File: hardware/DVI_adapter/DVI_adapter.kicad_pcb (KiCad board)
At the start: 2 copper layers, 34.6 x 28.4 mm, 51 parts, among them J1 DF12NB(3.0)-30DS-0.5V(51), J2 DF12NB(3.0)-30DS-0.5V(51), J3 FPC Cable connector 1x20, U2 TXS0102DQMR, U3 TFP410

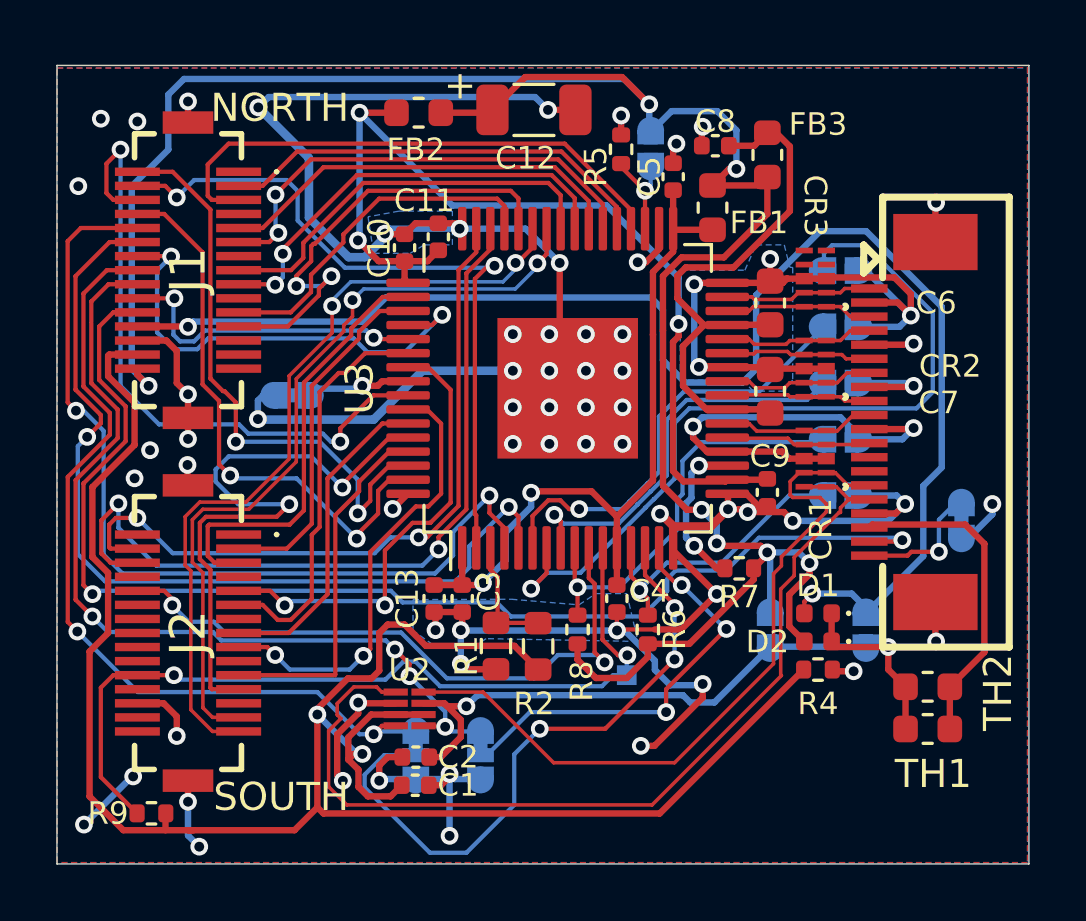
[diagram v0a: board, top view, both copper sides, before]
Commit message: Change to 4 layers for better signal integrity. Reorganize differential pins in SSG format to minimize crosstalk at output connector (pinout compatible with common extension cables). Fix level translator footpriont. Add power plane, test points, 5V charge pump, auto reset
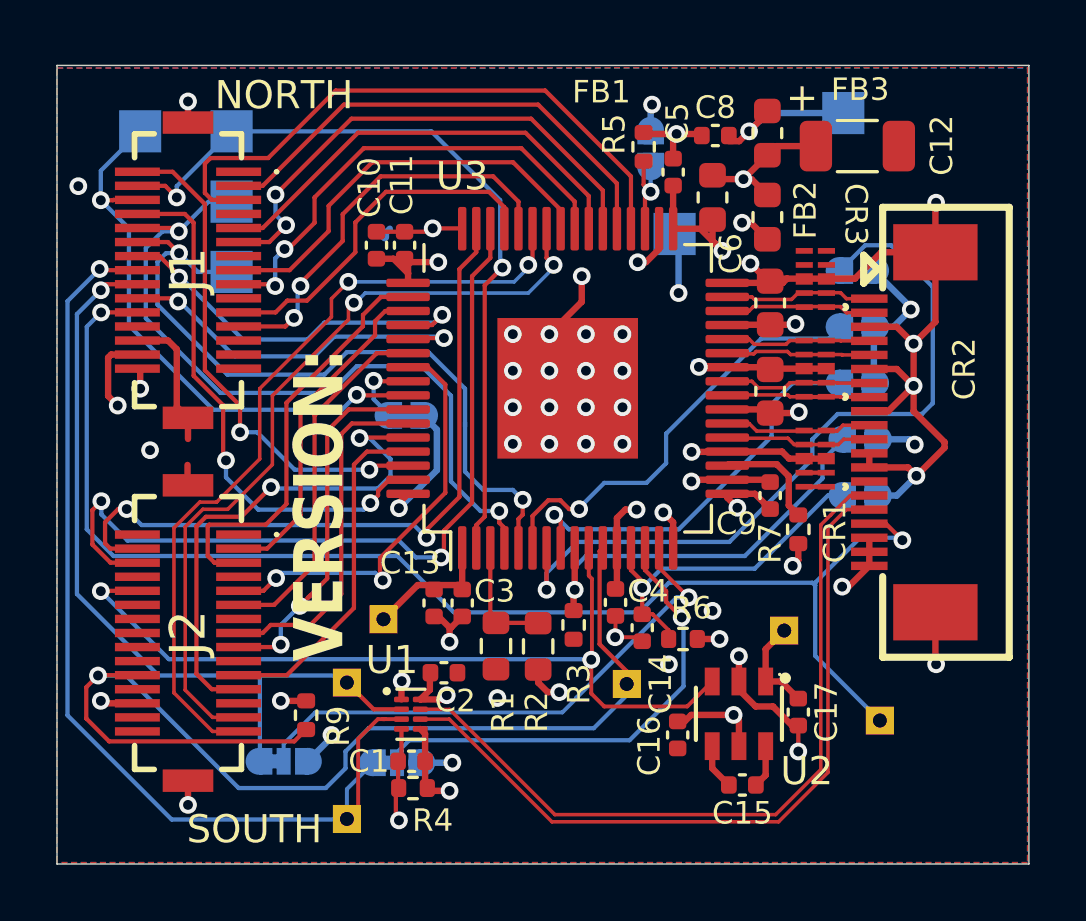
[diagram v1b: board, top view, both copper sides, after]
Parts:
- removed D1, D2: NSR05F40NXT5G, Diode_SMD:D_0402_1005Metric
- removed JP10, JP11: JMP_ISEL, Library:SolderJumper-2_Open_RoundedPad_2.254x0.95mm
- removed JP12: JMP_CKn, Library:SolderJumper-2_Closed_RoundedPad_2.254x0.95mm
- removed R8: 10K, Resistor_SMD:R_0402_1005Metric
- removed TH1, TH2: PRG18BB330MB1RB, Fuse:Fuse_0603_1608Metric
- added C14: 0.1uF, Library:C_0402_1005Metric, F.Cu at (124.5, 132.9)
- added C15: 2.2uF, Library:C_0402_1005Metric, F.Cu at (128.1, 138.5)
- added C16: 2.2uF, Library:C_0402_1005Metric, F.Cu at (125.8, 136.7)
- added C17: 2.2uF, Library:C_0402_1005Metric, F.Cu at (130.1, 135.9)
- added R3: 10K, Resistor_SMD:R_0402_1005Metric, F.Cu at (122.1, 132.8)
- added TP10: TP_SDA, TestPoint:TestPoint_THTPad_1.0x1.0mm_Drill0.5mm, B.Cu at (114.0, 139.7)
- added TP11: TP_SCK, TestPoint:TestPoint_THTPad_1.0x1.0mm_Drill0.5mm, B.Cu at (114.0, 134.8)
- added TP12: TP_HPD, TestPoint:TestPoint_THTPad_1.0x1.0mm_Drill0.5mm, B.Cu at (133.0, 136.2)
- added TP2: TP_DE, TestPoint:TestPoint_Pad_1.5x1.5mm, B.Cu at (110.0, 115.2)
- added TP3: TP_HS, TestPoint:TestPoint_Pad_1.5x1.5mm, B.Cu at (110.0, 117.8)
- added TP4: TP_VS, TestPoint:TestPoint_Pad_1.5x1.5mm, B.Cu at (110.0, 120.2)
- added TP5: TP_PCLK, TestPoint:TestPoint_Pad_1.5x1.5mm, B.Cu at (106.7, 115.2)
- added TP6: TP_PVDD, TestPoint:TestPoint_Pad_1.5x1.5mm, B.Cu at (125.7, 118.9)
- added TP7: TP_DVDD, TestPoint:TestPoint_THTPad_1.0x1.0mm_Drill0.5mm, B.Cu at (115.3, 132.6)
- added TP8: TP_TVDD, TestPoint:TestPoint_Pad_1.5x1.5mm, B.Cu at (131.7, 114.6)
- added TP9: TP_VDVI, TestPoint:TestPoint_THTPad_1.0x1.0mm_Drill0.5mm, B.Cu at (129.6, 133.0)
- added U1: TXS0102DQE, Package_SON:X2SON-8_1.4x1mm_P0.35mm, F.Cu at (116.3, 136.0)
- U2: value TXS0102DQMR -> HE9009M6R; footprint Library:DQM8 -> easyeda2kicad:SOT-23-6_L2.9-W1.7-P0.95-LS2.8-BL
- moved R4 15.0 mm to (116.4, 138.6), turned to 180 degrees
- moved G*** 13.2 mm to (107.0, 128.2), turned to 90 degrees
- moved FB2 12.9 mm to (129.0, 118.3), turned to -90 degrees
- moved U2 11.7 mm to (128.0, 136.0), turned to 180 degrees
- moved C12 11.6 mm to (132.2, 115.8)
- moved JP8 7.00 mm to (111.8, 137.7), turned to 0 degrees
- moved R9 6.51 mm to (112.6, 136.0), turned to -90 degrees
- moved JP9 4.12 mm to (116.2, 125.3), turned to 180 degrees
- moved C2 3.16 mm to (117.5, 134.5), turned to 0 degrees
- moved G*** 2.80 mm to (136.2, 117.0), turned to 90 degrees
- moved R7 2.52 mm to (130.1, 129.4), turned to -90 degrees
- moved R6 1.29 mm to (126.0, 133.3), turned to 0 degrees
- moved C11 1.24 mm to (116.1, 119.3)
- moved C10 1.00 mm to (115.1, 119.3)
- moved C1 0.86 mm to (116.3, 137.7), turned to 180 degrees
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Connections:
- CR1 pad 1: SDA_SHIFTED -> Net-(CR1-Pad1)
- CR1 pad 10: SDA_SHIFTED -> Net-(CR1-Pad1)
- CR1 pad 2: SCK_SHIFTED -> Net-(CR1-Pad2)
- CR1 pad 9: SCK_SHIFTED -> Net-(CR1-Pad2)
- J3 pad 11: GND -> /TXC-
- J3 pad 12: /TXC- -> GND
- J3 pad 13: unconnected-(J3-Pad13) -> GND
- J3 pad 17: GND -> HPD
- J3 pad 18: V_DVI_OUT -> V_DVI
- J3 pad 19: HPD -> V_DVI
- J3 pad 2: GND -> /TX2-
- J3 pad 20: Net-(JP12-B) -> V_DVI
- J3 pad 3: /TX2- -> GND
- J3 pad 5: GND -> /TX1-
- J3 pad 6: /TX1- -> GND
- J3 pad 8: GND -> /TX0-
- J3 pad 9: /TX0- -> GND
- JP1 pad 1: GND -> +3V3
- JP2 pad 1: GND -> +3V3
- JP3 pad 1: GND -> +3V3
- JP6 pad 1: GND -> +3V3
- U2 pad 1: SDA_SHIFTED -> V_DVI
- U2 pad 3: VCC3V3 -> PSEL
- U2 pad 4: SDA -> Net-(U2-CN)
- U2 pad 5: SCK -> +3V3
- U2 pad 6: VCC3V3 -> Net-(U2-CP)
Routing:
- net GND: track 166.2 -> 83.5 mm, vias 70 -> 46
- net VCCIN: track 51.4 -> 0.00 mm, vias 2 -> 0
- net VCC3V3: track 71.0 -> 39.8 mm, vias 2 -> 5
- net V_DVI_OUT: track 11.5 -> 0.00 mm
- net DVDD: track 26.7 -> 36.4 mm
- net HPD2: track 29.8 -> 39.3 mm, vias 2 -> 1
- net SDA_SHIFTED: track 34.7 -> 27.2 mm
- net PSEL: track 22.8 -> 30.0 mm
- net SDA: track 29.9 -> 36.5 mm, vias 2 -> 1
- net Net-(JP7-C): track 22.8 -> 17.0 mm, vias 3 -> 1
- net LCD_VSYNC: track 32.2 -> 26.4 mm
- net LCD_HSYNC: track 32.2 -> 27.1 mm
- net Net-(JP8-C): track 15.1 -> 19.8 mm, vias 3 -> 1
- net Net-(JP12-B): track 4.70 -> 0.00 mm, vias 1 -> 0
- net HPD: track 44.1 -> 48.0 mm
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- added copper zone on In2.Cu, net +3V3
- added copper zone on In2.Cu, net DVDD
- added copper zone on In1.Cu, net GND
- added copper zone on In2.Cu, net PVDD
- added copper zone on In2.Cu, net TVDD
- added copper zone on In2.Cu, net VCC3V3
- added copper zone on In2.Cu, net V_DVI
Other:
- copper layers 2 -> 4
- board text added: "DVI Adapter V0.1"
- board text added: "VERSION:"
- board text removed: "DVI Adapter V0.09"

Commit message: improve power plane in DVI adapter
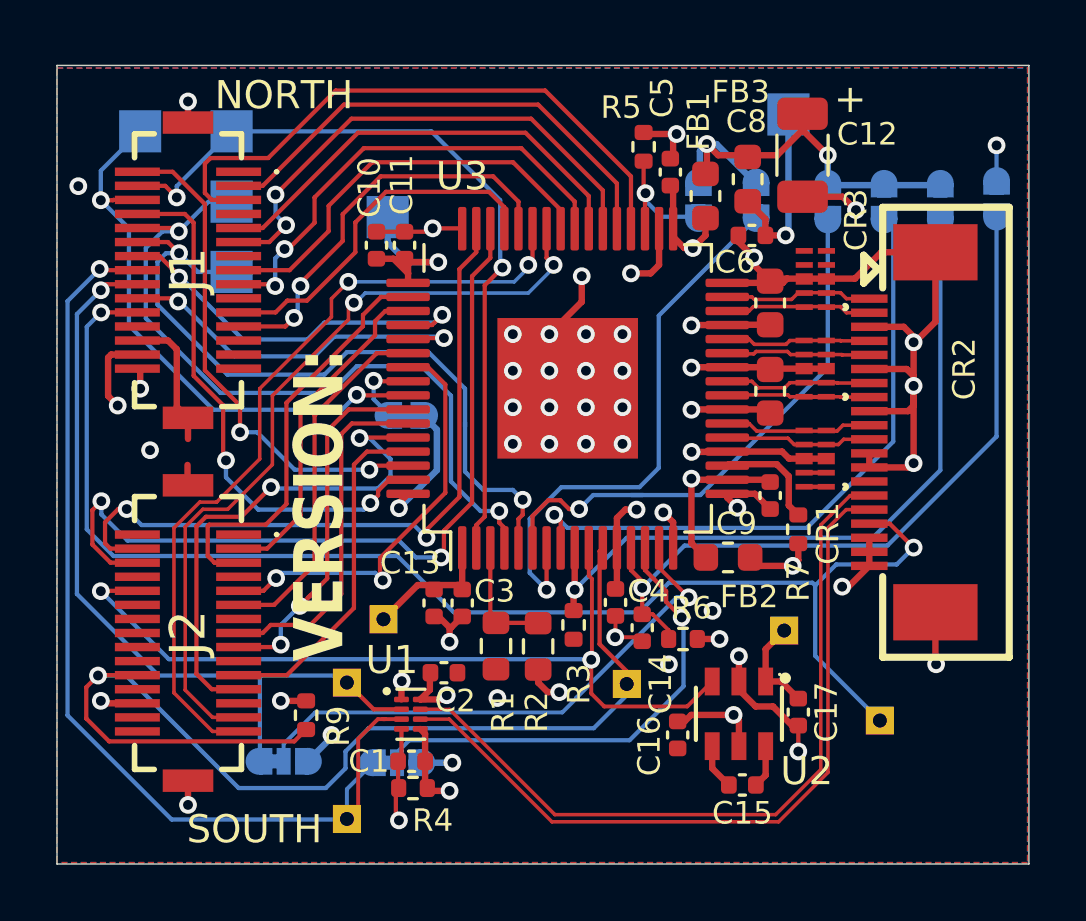
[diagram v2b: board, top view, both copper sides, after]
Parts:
- moved FB2 12.2 mm to (127.6, 130.4), turned to 180 degrees
- moved JP5 11.6 mm to (137.2, 117.7), turned to -90 degrees
- moved TP6 10.2 mm to (115.5, 118.3)
- moved JP6 8.92 mm to (135.2, 117.8), turned to -90 degrees
- moved JP3 6.52 mm to (133.2, 117.8), turned to -90 degrees
- moved JP1 4.57 mm to (131.2, 117.8), turned to -90 degrees
- moved JP2 4.38 mm to (128.6, 117.7), turned to -90 degrees
- moved C8 3.78 mm to (128.4, 119.0)
- moved G*** 2.78 mm to (134.8, 114.6), turned to 180 degrees
- moved JP4 2.50 mm to (126.5, 117.7)
- moved C12 1.98 mm to (130.2, 116.1), turned to -90 degrees
- moved TP8 1.95 mm to (129.8, 114.7)
- moved FB3 1.78 mm to (128.3, 117.0), turned to -90 degrees
- moved FB1 0.25 mm to (126.8, 117.5)
- moved C5 0.10 mm to (125.5, 116.7)
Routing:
- net +3V3: track 80.1 -> 55.1 mm, vias 8 -> 6
- net Net-(JP5-B): track 12.5 -> 26.7 mm
- net Net-(JP6-B): track 14.9 -> 26.0 mm
- net Net-(JP3-B): track 14.5 -> 22.9 mm
- net Net-(JP2-B): track 27.1 -> 20.0 mm
- net Net-(JP1-B): track 15.8 -> 19.9 mm
- net TVDD: track 21.2 -> 24.8 mm
- net PVDD: track 30.5 -> 27.8 mm, vias 4 -> 2
- net Net-(JP4-B): track 3.54 -> 4.82 mm
- net HPD: track 48.0 -> 49.1 mm
- net DVDD: track 36.4 -> 35.5 mm
- net GND: track 83.5 -> 83.8 mm, vias 46 -> 47
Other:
- board text added: "DVI Adapter v0.1"
- board text removed: "DVI Adapter V0.1"

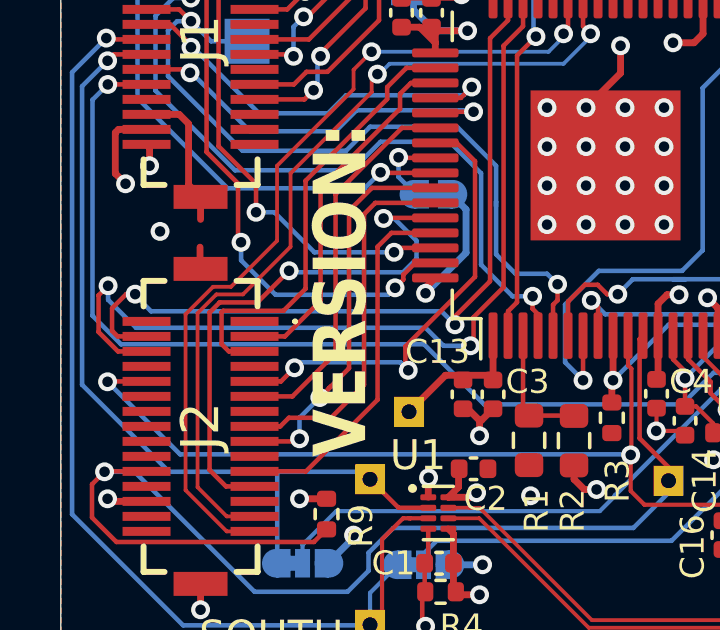
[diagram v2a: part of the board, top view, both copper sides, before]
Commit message: fixed mixup of pins G5/G4 (3rd diff pair ODD) and DE/PCLK (3rd diff pair EVEN), now with correct polarity for diff pairs
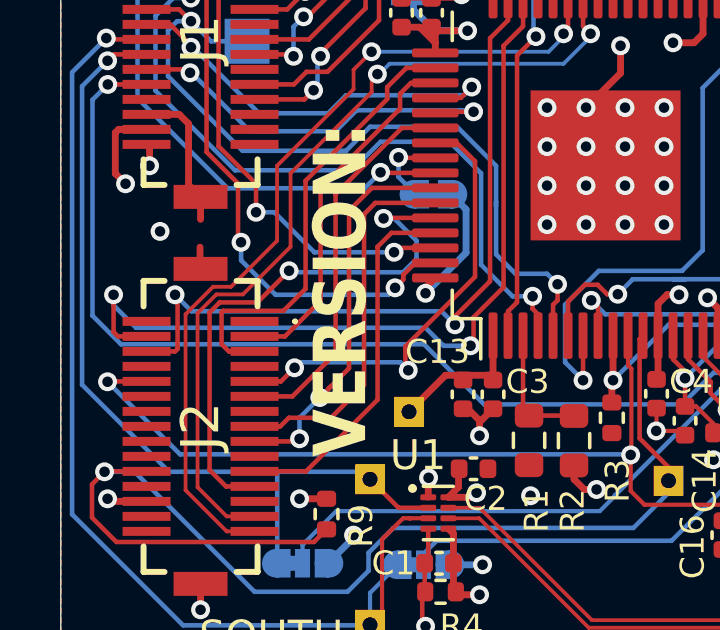
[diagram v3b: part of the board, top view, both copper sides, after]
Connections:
- J2 pad 4: G4 -> G5
- J2 pad 6: G5 -> G4
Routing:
- net G5: track 29.1 -> 27.6 mm
- net G4: track 25.8 -> 24.4 mm
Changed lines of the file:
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@@
 			)
 		)
-		(property "LCSC Part" "C5123433"
+		(property "Manufacturer" "HEERMICR(赫尔半导体)"
 			(at 0 0 180)
+			(unlocked yes)
 			(layer "F.Fab")
 			(hide yes)
 			(effects
 				(font
-					(size 1.27 1.27)
+					(size 1 1)
 					(thickness 0.15)
 				)
 			)
 		)
-		(property "Manufacturer" "HEERMICR(赫尔半导体)"
+		(property "MPN" "HE9009M6R"
 			(at 0 0 180)
 			(unlocked yes)
@@
 			)
 		)
-		(property "MPN" "HE9009M6R"
+		(property "MPN_ALT" "AP3602A"
 			(at 0 0 180)
 			(unlocked yes)
@@
 			(net 49 "unconnected-(J2-1-Pad2)")
 			(pinfunction "1")
-			(pintype "passive+no_connect")
+			(pintype "passive")
 		)
 		(pad "3" smd rect
@@
 			(size 0.3 1.6)
 			(layers "F.Cu" "F.Paste" "F.Mask")
-			(net 22 "G4")
+			(net 24 "G5")
 			(pinfunction "3")
 			(pintype "passive")
@@
 			(size 0.3 1.6)
 			(layers "F.Cu" "F.Paste" "F.Mask")
-			(net 24 "G5")
+			(net 22 "G4")
 			(pinfunction "5")
 			(pintype "passive")
@@
 			)
 		)
+		(property ki_fp_filters "SolderJumper*Open*")
+		(sheetname "Root")
+		(sheetfile "DVI_adapter.kicad_sch")
 		(attr exclude_from_pos_files)
 		(fp_line
@@
 			)
 		)
+		(property ki_fp_filters "SolderJumper*Open*")
+		(sheetname "Root")
+		(sheetfile "DVI_adapter.kicad_sch")
 		(attr exclude_from_pos_files)
 		(fp_line
@@
 			)
 		)
+		(property ki_fp_filters "SolderJumper*Open*")
+		(sheetname "Root")
+		(sheetfile "DVI_adapter.kicad_sch")
 		(attr exclude_from_pos_files)
 		(fp_line
@@
 			)
 		)
+		(property ki_fp_filters "SolderJumper*Open*")
+		(sheetname "Root")
+		(sheetfile "DVI_adapter.kicad_sch")
 		(attr exclude_from_pos_files)
 		(fp_line
@@
 			)
 		)
+		(property ki_fp_filters "SolderJumper*Open*")
+		(sheetname "Root")
+		(sheetfile "DVI_adapter.kicad_sch")
 		(attr exclude_from_pos_files)
 		(fp_line
@@
 	)
 	(segment
-		(start 105.920498 128.679502)
-		(end 105.45 129.15)
+		(start 107.6333 130.5066)
+		(end 107.6333 128.7833)
 		(width 0.1524)
 		(layer "F.Cu")
@@
 	)
 	(segment
-		(start 105.45 129.9)
-		(end 105.6375 130.0875)
-		(width 0.1524)
-		(layer "F.Cu")
-		(net 22)
-	)
-	(segment
 		(start 118.65 119.55)
 		(end 118.65 118.7125)
@@
 	)
 	(segment
-		(start 106.220498 128.679502)
-		(end 105.920498 128.679502)
+		(start 106.6 130.5875)
+		(end 107.5524 130.5875)
 		(width 0.1524)
 		(layer "F.Cu")
@@
 	)
 	(segment
-		(start 105.45 129.15)
-		(end 105.45 129.9)
+		(start 107.5524 130.5875)
+		(end 107.6333 130.5066)
 		(width 0.1524)
 		(layer "F.Cu")
@@
 	)
 	(segment
-		(start 105.6375 130.0875)
-		(end 106.6 130.0875)
+		(start 107.6333 128.7833)
+		(end 107.55 128.7)
 		(width 0.1524)
 		(layer "F.Cu")
@@
 	)
 	(via
-		(at 106.220498 128.679502)
+		(at 107.55 128.7)
 		(size 0.63)
 		(drill 0.35)
@@
 	)
 	(segment
-		(start 106.75 129.25)
-		(end 116.4318 129.25)
+		(start 107.55 128.7)
+		(end 108.1 129.25)
 		(width 0.1524)
 		(layer "B.Cu")
@@
 	)
 	(segment
-		(start 106.220498 128.679502)
-		(end 106.220498 128.720498)
-		(width 0.1524)
-		(layer "B.Cu")
-		(net 22)
-	)
-	(segment
-		(start 106.220498 128.720498)
-		(end 106.75 129.25)
+		(start 108.1 129.25)
+		(end 116.4318 129.25)
 		(width 0.1524)
 		(layer "B.Cu")
@@
 	)
 	(segment
-		(start 105 128.7182)
-		(end 105 129.9399)
+		(start 105.6476 130.0875)
+		(end 106.6 130.0875)
+		(width 0.1524)
+		(layer "F.Cu")
+		(net 24)
+	)
+	(segment
+		(start 105.5 128.7)
+		(end 105.5 129.9399)
 		(width 0.1524)
 		(layer "F.Cu")
@@
 	)
 	(segment
-		(start 105.6476 130.5875)
-		(end 106.6 130.5875)
+		(start 105.5 129.9399)
+		(end 105.6476 130.0875)
 		(width 0.1524)
 		(layer "F.Cu")
@@
 	)
 	(segment
-		(start 105 129.9399)
-		(end 105.6476 130.5875)
-		(width 0.1524)
-		(layer "F.Cu")
-		(net 24)
-	)
-	(segment
 		(start 117.4 130.4)
 		(end 117.5 130.3)
@@
 		(net 24)
 	)
-	(segment
-		(start 105.3182 128.4)
-		(end 105 128.7182)
-		(width 0.1524)
-		(layer "F.Cu")
-		(net 24)
-	)
 	(via
 		(at 117.4 130.4)
@@
 	)
 	(via
-		(at 105.3182 128.4)
+		(at 105.5 128.7)
 		(size 0.63)
 		(drill 0.35)
@@
 	)
 	(segment
-		(start 106.25 129.8)
-		(end 115.9 129.8)
+		(start 116.5 130.4)
+		(end 117.4 130.4)
 		(width 0.1524)
 		(layer "B.Cu")
@@
 	)
 	(segment
-		(start 105.3182 128.4)
-		(end 105.3182 128.8682)
+		(start 105.5 129.05)
+		(end 106.25 129.8)
 		(width 0.1524)
 		(layer "B.Cu")
@@
 	)
 	(segment
-		(start 115.9 129.8)
-		(end 116.5 130.4)
+		(start 106.25 129.8)
+		(end 115.9 129.8)
 		(width 0.1524)
 		(layer "B.Cu")
@@
 	)
 	(segment
-		(start 116.5 130.4)
-		(end 117.4 130.4)
+		(start 115.9 129.8)
+		(end 116.5 130.4)
 		(width 0.1524)
 		(layer "B.Cu")
@@
 	)
 	(segment
-		(start 105.3182 128.8682)
-		(end 106.25 129.8)
+		(start 105.5 128.7)
+		(end 105.5 129.05)
 		(width 0.1524)
 		(layer "B.Cu")
